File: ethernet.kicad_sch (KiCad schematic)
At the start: 32 parts, among them J201 8P8C_Shielded, SW201 SW_SPDT, U201 DP83826ERHBR, Y201 25Mhz

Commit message: layout re-design start
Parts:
- Y201: footprint Crystal:Crystal_SMD_HC49-SD_HandSoldering -> Crystal:Crystal_SMD_HC49-SD
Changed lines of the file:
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@@
 			)
 		)
-		(property "Footprint" "Crystal:Crystal_SMD_HC49-SD_HandSoldering"
+		(property "Footprint" "Crystal:Crystal_SMD_HC49-SD"
 			(at 54.4056 101.5604 0)
 			(effects

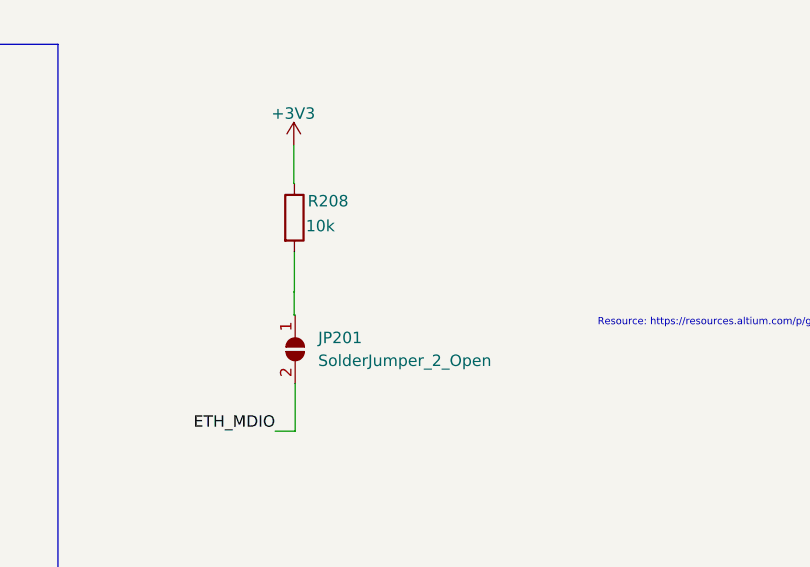
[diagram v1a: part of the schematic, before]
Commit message: ethernet, debugger and usb layouts re-designed
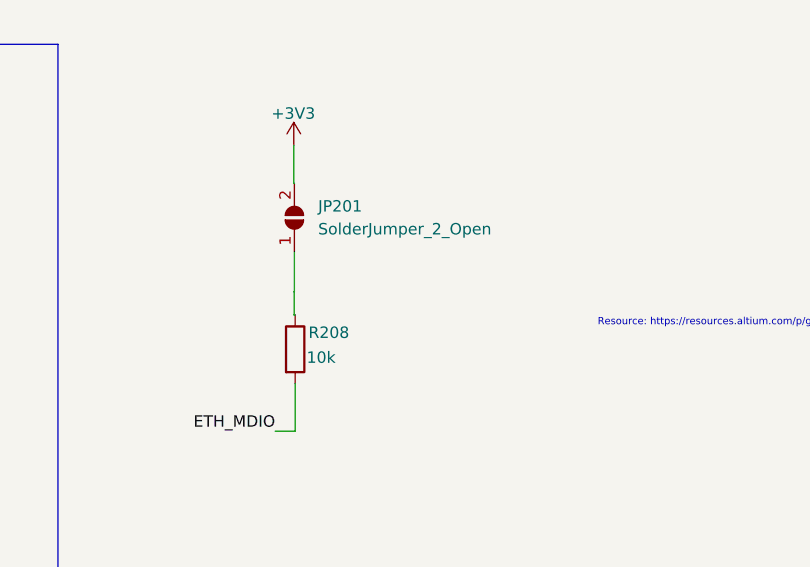
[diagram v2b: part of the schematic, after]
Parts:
- SW201: footprint footprints:SW_PTS636_SM43J_SMTR_LFS -> Button_Switch_SMD:SW_SPST_B3U-1000P
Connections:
- net +3V3: now also JP201.2 (B); no longer R208.1
- net ETH_MDIO: now also R208.2; no longer JP201.2 (B)
- net at JP201.1 (A): now also R208.1; no longer R208.2
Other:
- moved on the sheet: JP201, R208
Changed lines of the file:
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@@
 			)
 		)
-		(property "Footprint" "footprints:SW_PTS636_SM43J_SMTR_LFS"
+		(property "Footprint" "Button_Switch_SMD:SW_SPST_B3U-1000P"
 			(at 180.3261 46.8577 0)
 			(effects
@@
 	(symbol
 		(lib_id "Device:R")
-		(at 147.2259 152.3269 0)
+		(at 147.3112 166.9429 0)
 		(unit 1)
 		(exclude_from_sim no)
@@
 		(dnp no)
 		(property "Reference" "R208"
-			(at 148.7016 150.4816 0)
+			(at 148.7869 165.0976 0)
 			(effects
 				(font
@@
 		)
 		(property "Value" "10k"
-			(at 148.4967 153.2469 0)
+			(at 148.582 167.8629 0)
 			(effects
 				(font
@@
 		)
 		(property "Footprint" "Resistor_SMD:R_0805_2012Metric_Pad1.20x1.40mm_HandSolder"
-			(at 145.4479 152.3269 90)
+			(at 145.5332 166.9429 90)
 			(effects
 				(font
@@
 		)
 		(property "Datasheet" "~"
-			(at 147.2259 152.3269 0)
+			(at 147.3112 166.9429 0)
 			(effects
 				(font
@@
 		)
 		(property "Description" "Resistor"
-			(at 147.2259 152.3269 0)
+			(at 147.3112 166.9429 0)
 			(effects
 				(font
@@
 	(symbol
 		(lib_id "Jumper:SolderJumper_2_Open")
-		(at 147.3112 166.9429 270)
+		(at 147.2259 152.3269 90)
 		(unit 1)
 		(exclude_from_sim no)
@@
 		(fields_autoplaced yes)
 		(property "Reference" "JP201"
-			(at 149.86 165.6728 90)
-			(effects
-				(font
-					(size 1.27 1.27)
-				)
-				(justify left)
+			(at 149.86 151.0568 90)
+			(effects
+				(font
+					(size 1.27 1.27)
+				)
+				(justify right)
 			)
 		)
 		(property "Value" "SolderJumper_2_Open"
-			(at 149.86 168.2128 90)
-			(effects
-				(font
-					(size 1.27 1.27)
-				)
-				(justify left)
+			(at 149.86 153.5968 90)
+			(effects
+				(font
+					(size 1.27 1.27)
+				)
+				(justify right)
 			)
 		)
 		(property "Footprint" "Jumper:SolderJumper-2_P1.3mm_Open_RoundedPad1.0x1.5mm"
-			(at 147.3112 166.9429 0)
+			(at 147.2259 152.3269 0)
 			(effects
 				(font
@@
 		)
 		(property "Datasheet" "~"
-			(at 147.3112 166.9429 0)
+			(at 147.2259 152.3269 0)
 			(effects
 				(font
@@
 		)
 		(property "Description" "Solder Jumper, 2-pole, open"
-			(at 147.3112 166.9429 0)
-			(effects
-				(font
+			(at 147.2259 152.3269 0)
+			(effects
+				(font

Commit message: some additions
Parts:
- renumbered C202 to C?, C201 to C?, C207 to C?, C211 to C?, C203 to C?, C209 to C?, C210 to C?, C212 to C?, C206 to C?, C205 to C?, C204 to C?, C208 to C?, D204 to D?, D202 to D?, D206 to D?, D201 to D?, D205 to D?, D203 to D?, FB201 to FB?, J201 to J?, JP201 to JP?, R207 to R?, R208 to R?, R202 to R?, R206 to R?, R201 to R?, R203 to R?, R205 to R?, R204 to R?, SW201 to SW?, U201 to U?, Y201 to Y?
